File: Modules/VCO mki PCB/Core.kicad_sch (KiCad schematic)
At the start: 38 parts, among them Q1 BC558, Q2 BC548, U1 40106, U2 TL074

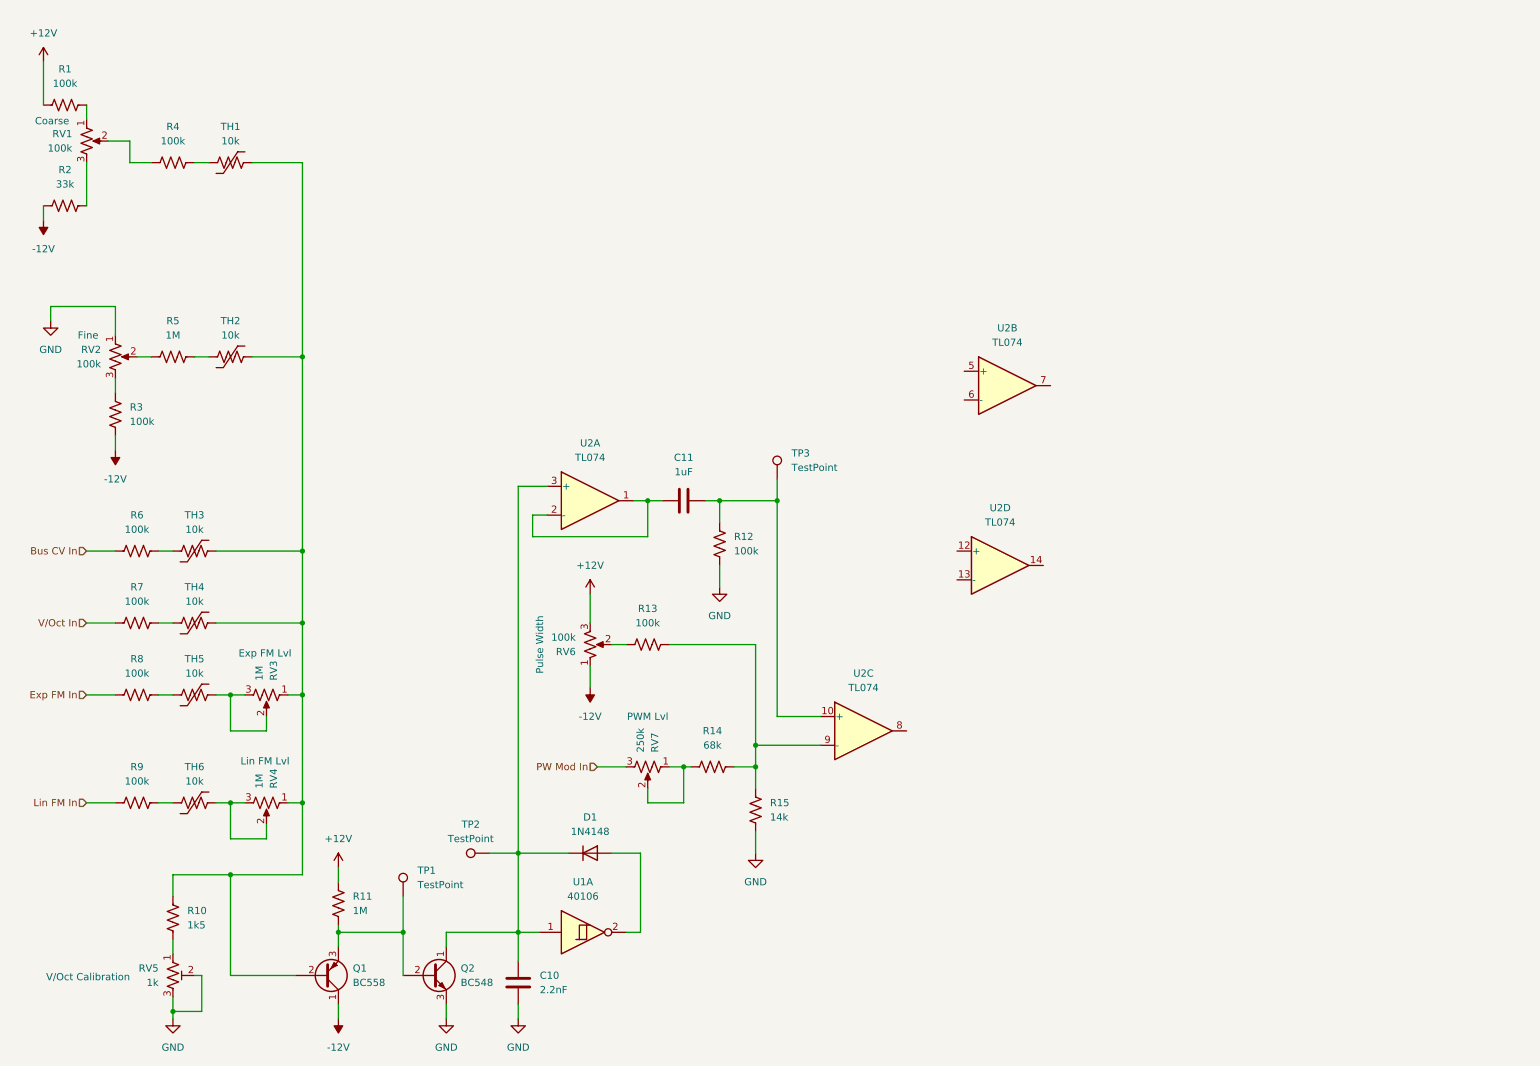
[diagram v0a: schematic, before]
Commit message: Designed VCO core and saw-to-tri circuits
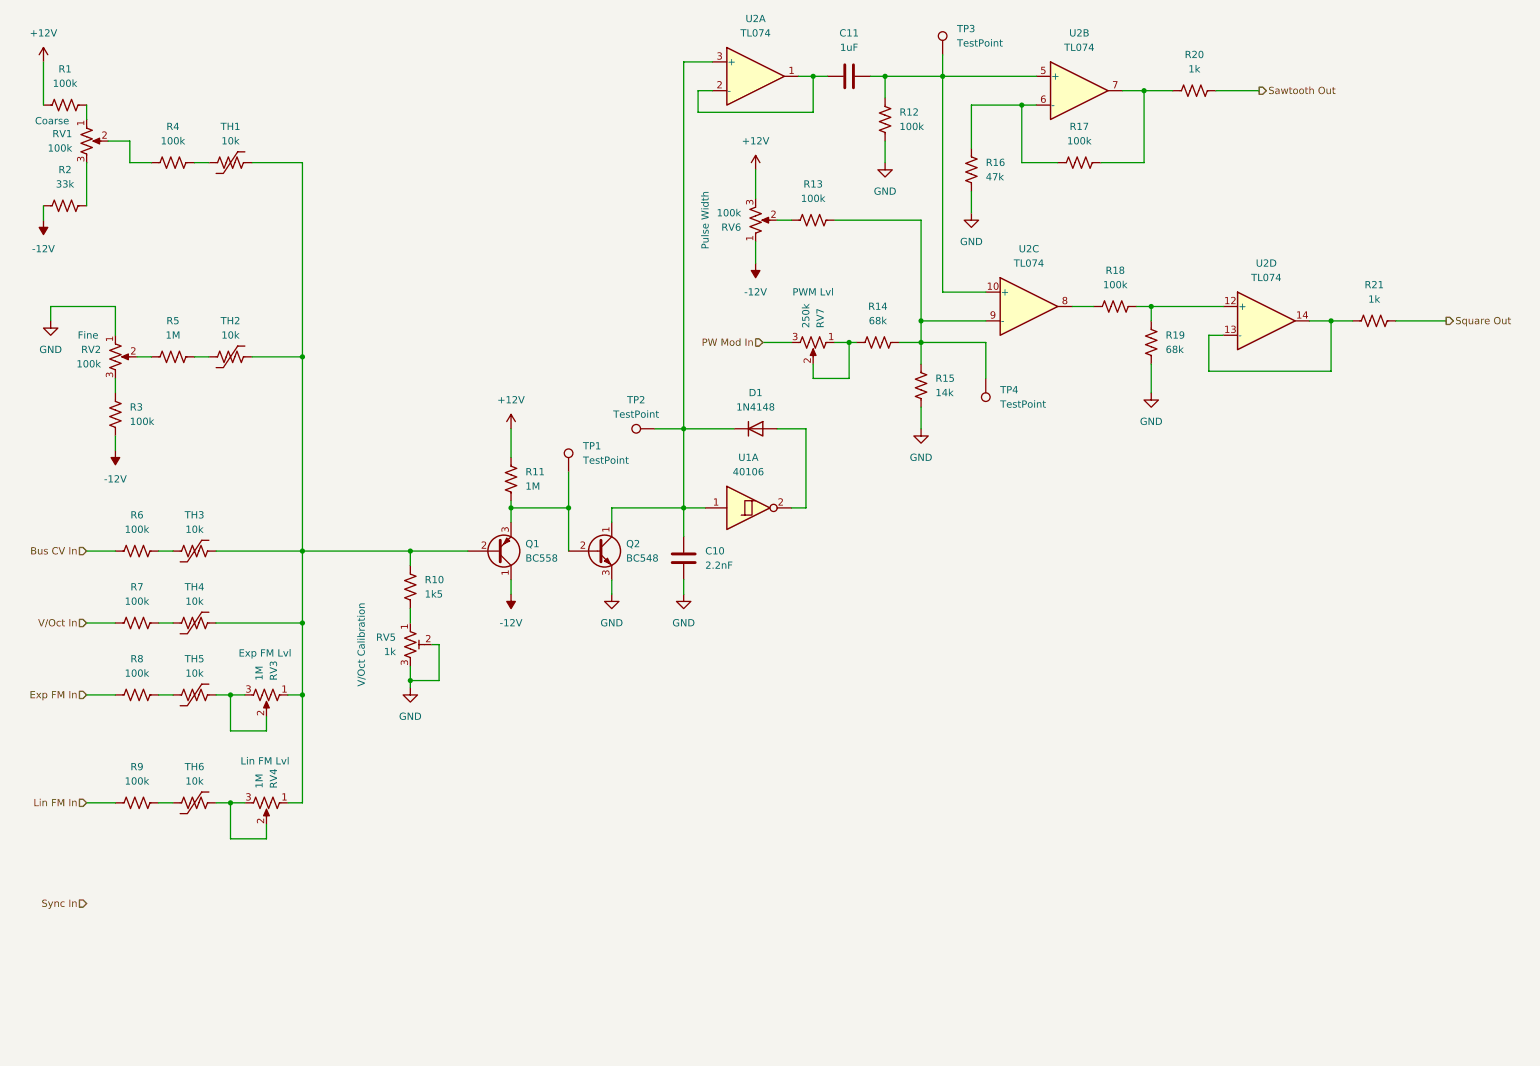
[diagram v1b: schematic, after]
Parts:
- added R16: 47k, Resistor_THT:R_Axial_DIN0204_L3.6mm_D1.6mm_P5.08mm_Horizontal, symbol Device:R_US
- added R17, R18: 100k, Resistor_THT:R_Axial_DIN0204_L3.6mm_D1.6mm_P5.08mm_Horizontal, symbol Device:R_US
- added R19: 68k, Resistor_THT:R_Axial_DIN0204_L3.6mm_D1.6mm_P5.08mm_Horizontal, symbol Device:R_US
- added R20, R21: 1k, Resistor_THT:R_Axial_DIN0204_L3.6mm_D1.6mm_P5.08mm_Horizontal, symbol Device:R_US
- added TP4: TestPoint, symbol Connector:TestPoint
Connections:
- net GND: now also R16.1, R19.2
- net at C11.2, R12.2, TP3.1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: now also U2.5 (+)
- net at R13.1, R14.1, R15.1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: now also TP4.1
- net at U2.6 (-): now also R16.2, R17.2
- net at U2.7: now also R17.1, R20.2
- net at U2.12 (+): now also R18.1, R19.1
- net at U2.13 (-): now also U2.14, R21.2
- net at U2.8: now also R18.2
- new net Sawtooth Out: R20.1
- new net Square Out: R21.1
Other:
- moved on the sheet: C10, C11, D1, Q1, Q2, R10, R11, R12, R13, R14, R15, RV5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
